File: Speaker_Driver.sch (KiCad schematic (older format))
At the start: 46 parts

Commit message: Annotation has been done
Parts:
- gave numbers to parts that had none: 46

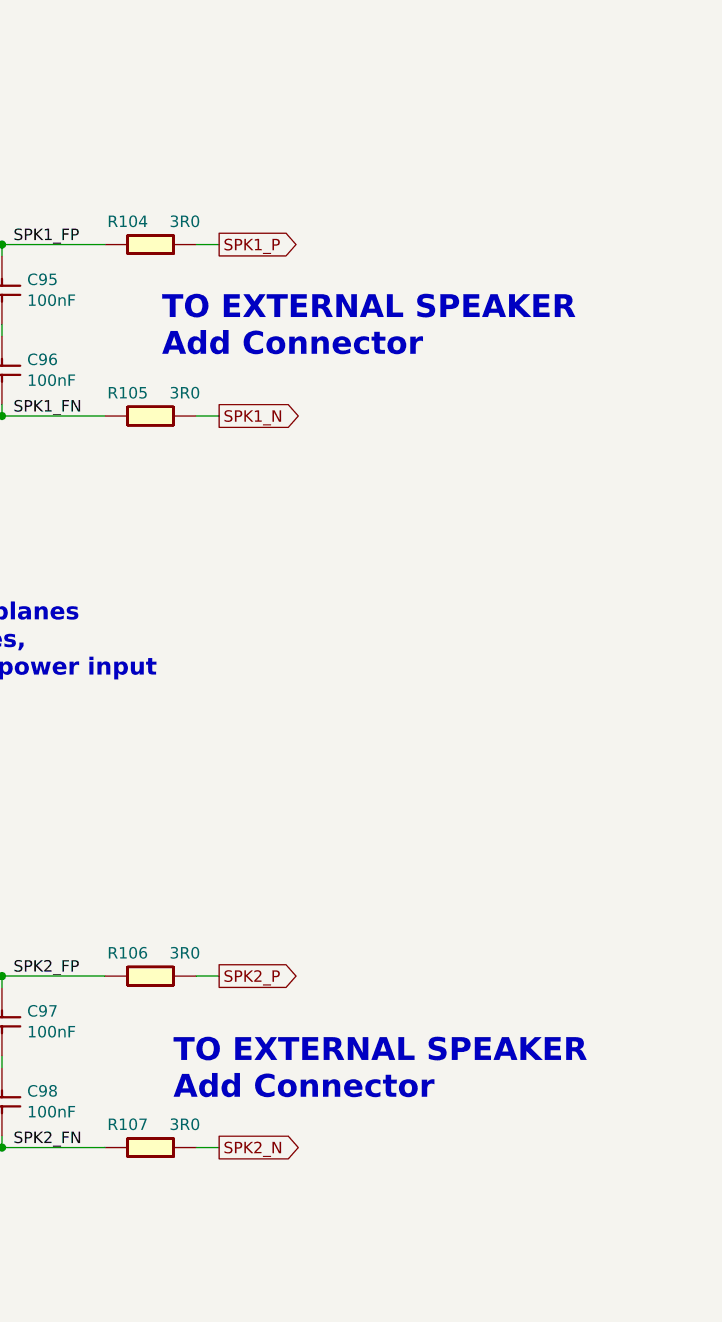
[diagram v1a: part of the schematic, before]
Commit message: added connectors for oxygen sensor and speakers molex 2.54mm pitch vertical
connectors have been added for oxygen sensor and speakers. thery are molex vertical connector 2.54mm pitch vertical. please let me know if any other part is desirable to be used instead.
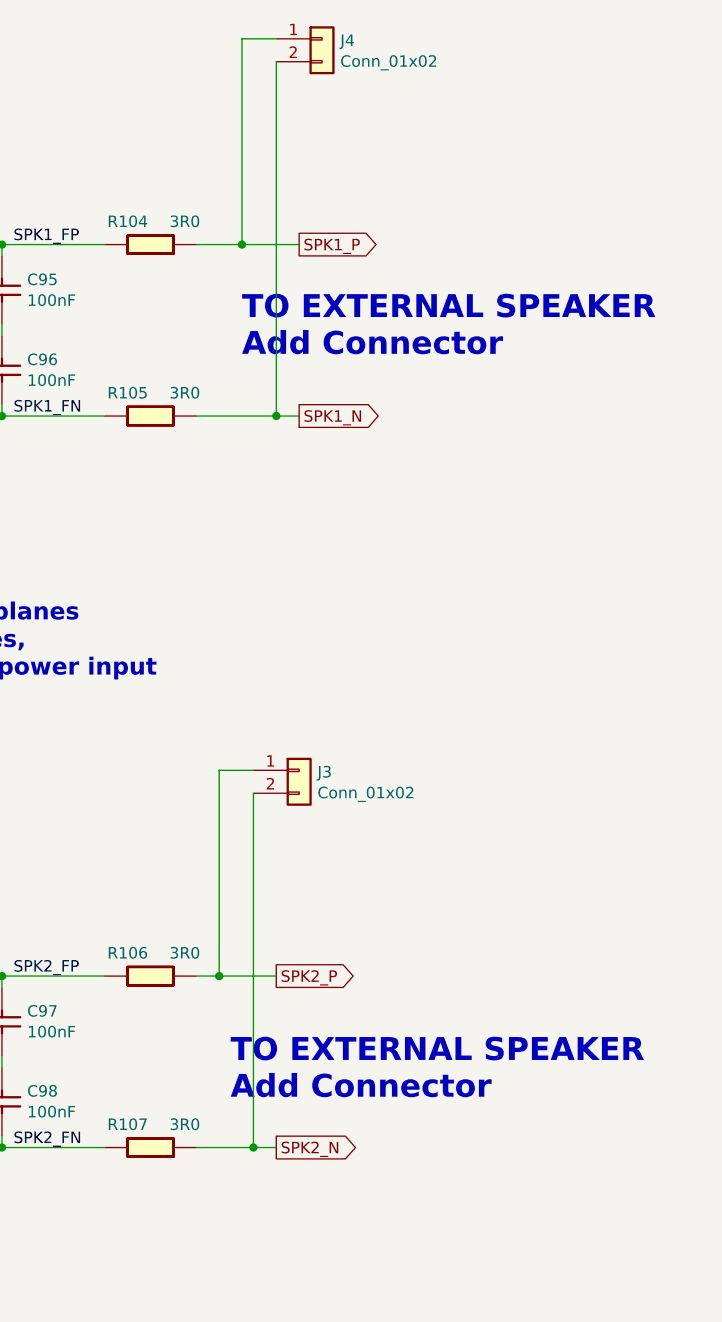
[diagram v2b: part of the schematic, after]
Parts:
- added J3, J4: Conn_01x02, Connector_PinSocket_2.54mm:PinSocket_1x02_P2.54mm_Vertical, symbol Connector_Generic:Conn_01x02
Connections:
- net SPK1_N: now also J4.2 (Pin_2)
- net SPK1_P: now also J4.1 (Pin_1)
- net SPK2_N: now also J3.2 (Pin_2)
- net SPK2_P: now also J3.1 (Pin_1)
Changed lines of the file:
@@
 	1    0    0    -1
 $EndComp
-Text GLabel 9300 1650 2    50   Output ~ 0
+Text GLabel 9650 1650 2    50   Output ~ 0
 SPK1_P
-Text GLabel 9300 2400 2    50   Output ~ 0
+Text GLabel 9650 2400 2    50   Output ~ 0
 SPK1_N
 Wire Wire Line
@@
 Connection ~ 8350 2400
 Wire Wire Line
-	9200 2400 9300 2400
-Wire Wire Line
 	8350 1650 8800 1650
 Connection ~ 8350 1650
-Wire Wire Line
-	9200 1650 9300 1650
 Text Label 8400 1650 0    50   ~ 0
 SPK1_FP
@@
 	1    0    0    -1
 $EndComp
-Text GLabel 9300 4850 2    50   Output ~ 0
+Text GLabel 9550 4850 2    50   Output ~ 0
 SPK2_P
-Text GLabel 9300 5600 2    50   Output ~ 0
+Text GLabel 9550 5600 2    50   Output ~ 0
 SPK2_N
 Wire Wire Line
@@
 Connection ~ 8350 5600
 Wire Wire Line
-	9200 5600 9300 5600
-Wire Wire Line
 	8350 4850 8800 4850
 Connection ~ 8350 4850
-Wire Wire Line
-	9200 4850 9300 4850
 Text Label 8400 4850 0    50   ~ 0
 SPK2_FP
@@
 	1    0    0    -1
 $EndComp
-Text Notes 9050 2150 0    100  ~ 20
+Text Notes 9400 2150 0    100  ~ 20
 TO EXTERNAL SPEAKER\nAdd Connector
 Text Notes 3500 7000 0    50   ~ 0
@@
 	6250 4250 6250 4300
 Connection ~ 6250 4300
-Text Notes 9100 5400 0    100  ~ 20
+Text Notes 9350 5400 0    100  ~ 20
 TO EXTERNAL SPEAKER\nAdd Connector
 Text Notes 600  1650 0    75   ~ 0
@@
 	1    0    0    -1
 $EndComp
+Wire Wire Line
+	9550 750  9400 750
+$Comp
+L Connector_Generic:Conn_01x02 J?
+U 1 1 6093A155
+P 9650 3950
+AR Path="/5F8F3873/6093A155" Ref="J?"  Part="1"
+AR Path="/60D4F569/6093A155" Ref="J3"  Part="1"
+F 0 "J3" H 9730 3942 50  0000 L CNN
+F 1 "Conn_01x02" H 9730 3851 50  0000 L CNN
+F 2 "Connector_PinSocket_2.54mm:PinSocket_1x02_P2.54mm_Vertical" H 9650 3950 50  0001 C CNN
+F 3 "http://www.farnell.com/datasheets/2695416.pdf" H 9650 3950 50  0001 C CNN
+	1    9650 3950
+	1    0    0    -1
+$EndComp
+Wire Wire Line
+	9450 3950 9300 3950
+Wire Wire Line
+	9200 4850 9300 4850
+Wire Wire Line
+	9200 5600 9450 5600
+Wire Wire Line
+	9200 1650 9400 1650
+Wire Wire Line
+	9200 2400 9550 2400
+Wire Wire Line
+	9550 850  9550 2400
+Connection ~ 9550 2400
+Wire Wire Line
+	9550 2400 9650 2400
+Wire Wire Line
+	9400 750  9400 1650
+Connection ~ 9400 1650
+Wire Wire Line
+	9400 1650 9650 1650
+Wire Wire Line
+	9450 4050 9450 5600
+Connection ~ 9450 5600
+Wire Wire Line
+	9450 5600 9550 5600
+Wire Wire Line
+	9300 3950 9300 4850
+Connection ~ 9300 4850
+Wire Wire Line
+	9300 4850 9550 4850
+$Comp
+L Connector_Generic:Conn_01x02 J?
+U 1 1 6099F86B
+P 9750 750
+AR Path="/5F8F3873/6099F86B" Ref="J?"  Part="1"
+AR Path="/60D4F569/6099F86B" Ref="J4"  Part="1"
+F 0 "J4" H 9830 742 50  0000 L CNN
+F 1 "Conn_01x02" H 9830 651 50  0000 L CNN
+F 2 "Connector_PinSocket_2.54mm:PinSocket_1x02_P2.54mm_Vertical" H 9750 750 50  0001 C CNN
+F 3 "http://www.farnell.com/datasheets/2695416.pdf" H 9750 750 50  0001 C CNN
+	1    9750 750
+	1    0    0    -1
+$EndComp

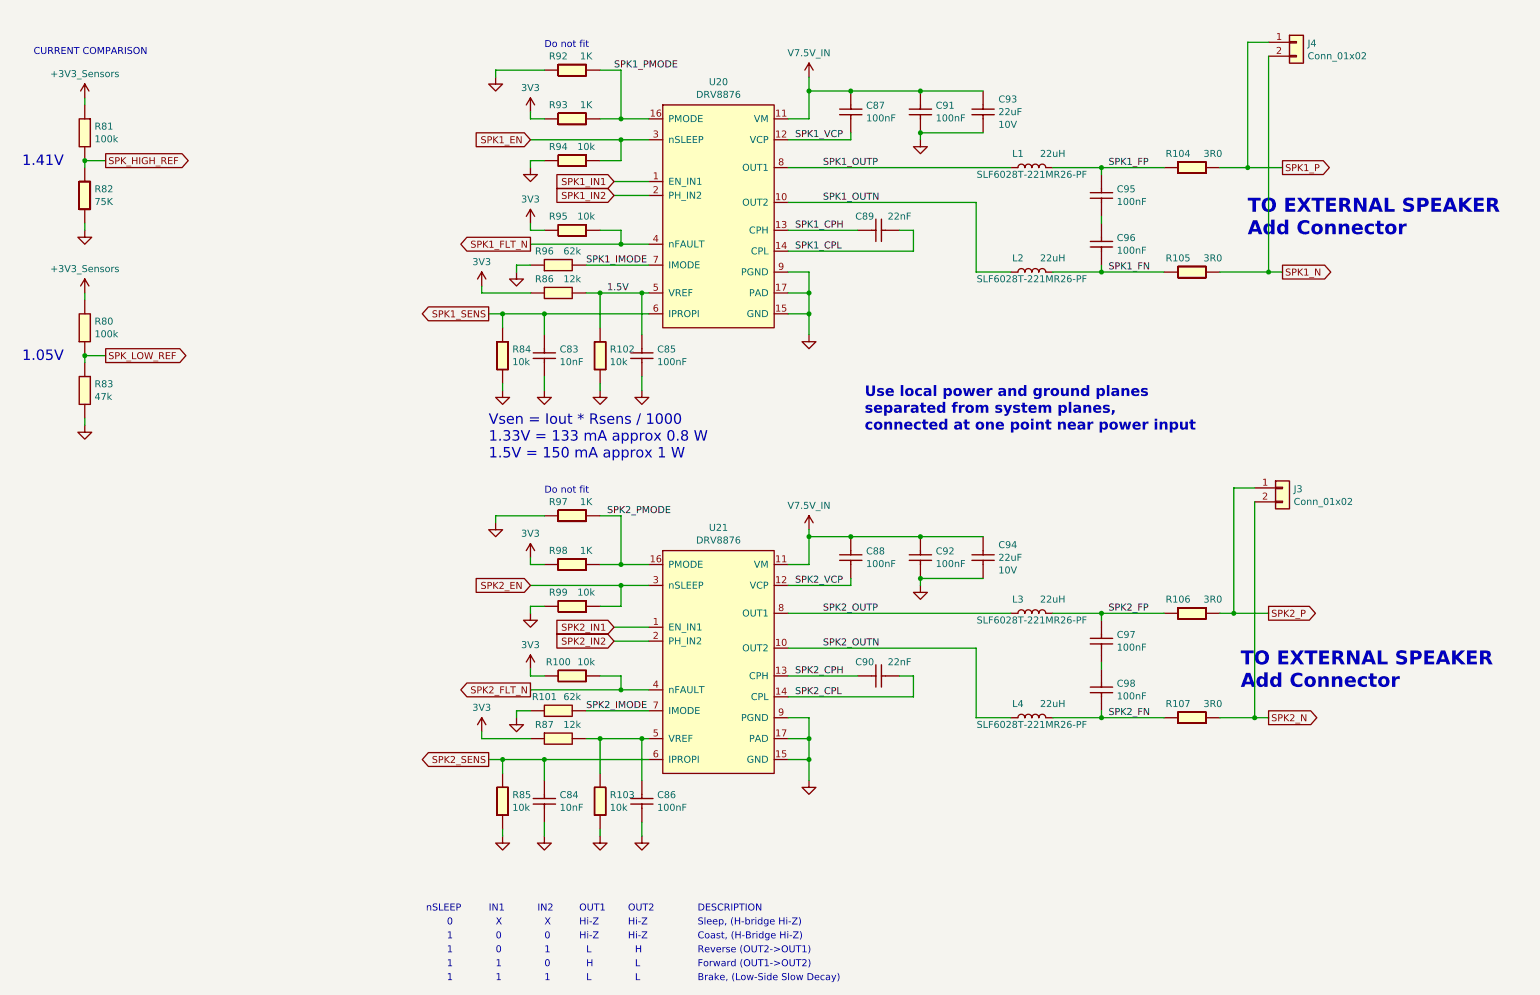
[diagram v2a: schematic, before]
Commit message: Task OEF-413 added zero ohm jumpers for 5V and 7.5V power supply to speaker driver circuits
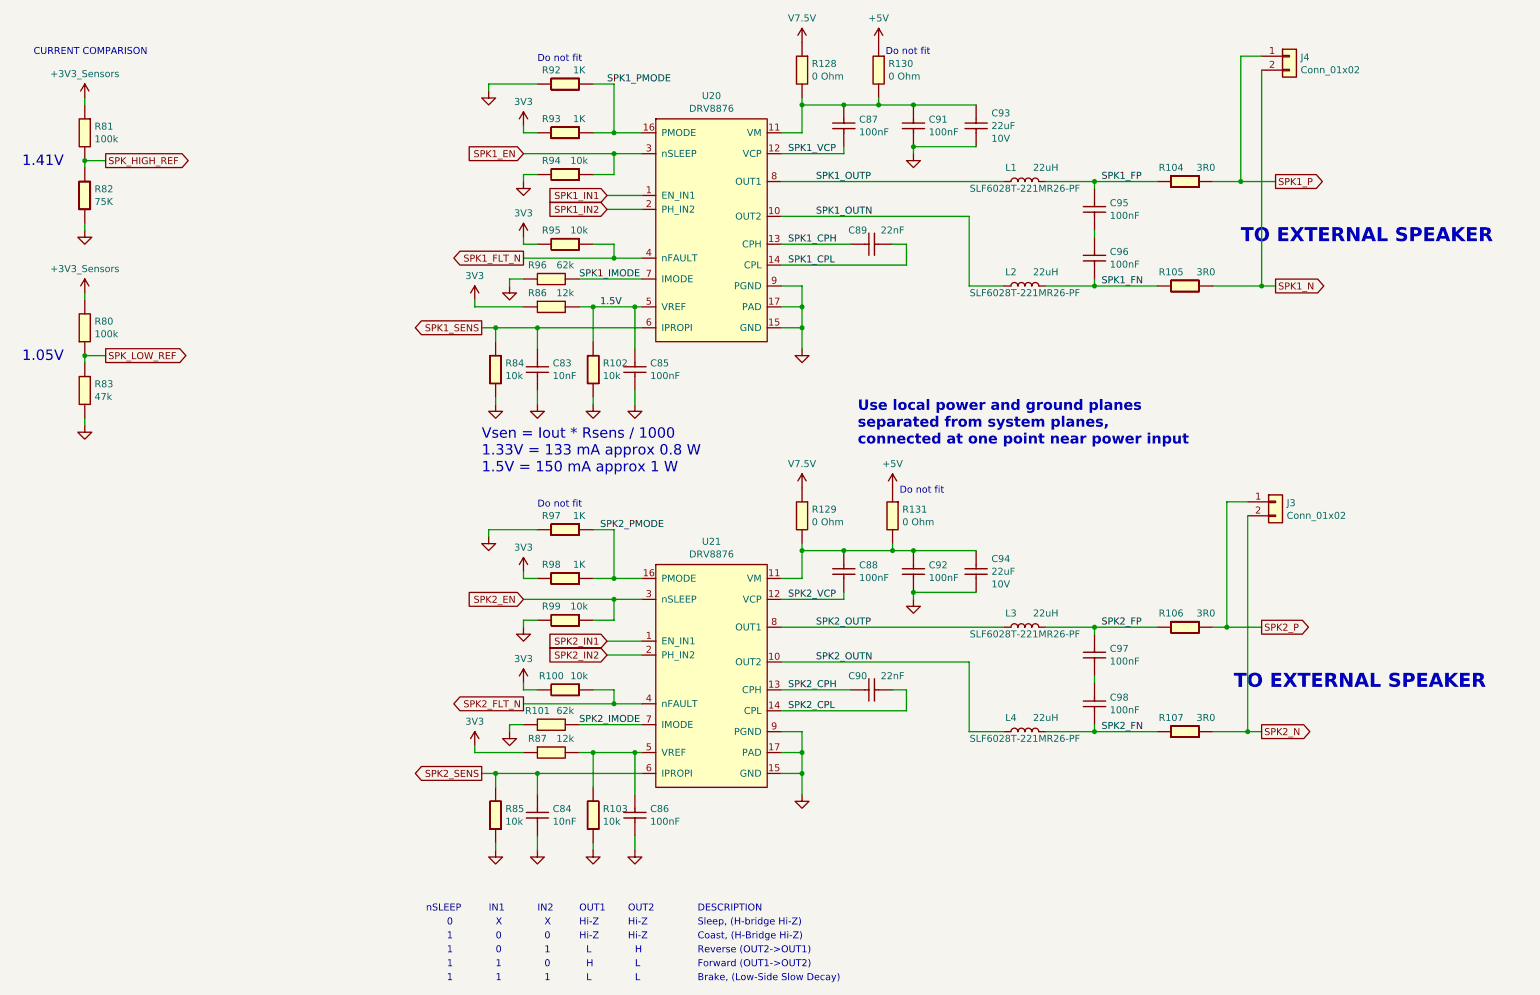
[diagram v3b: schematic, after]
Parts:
- added R128, R129, R130, R131: 0R0_0603_Chip_Resistor,_1%,_0.1W, symbol OpenVent:0R0_0603_Chip_Resistor,_1%,_0.1W
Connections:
- net +5V: now also R128.1, R129.1, R130.1, R131.1; no longer C87.1, C88.1, C91.1, C92.1, C93.1, C94.1, U20.11 (VM), U21.11 (VM)
- new net: C87.1, C91.1, C93.1, R128.2, R130.2, U20.11 (VM)
- new net: C88.1, C92.1, C94.1, R129.2, R131.2, U21.11 (VM)
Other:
- note added: "TO EXTERNAL SPEAKER"
- note removed: "TO EXTERNAL SPEAKER\nAdd Connector"
- moved on the sheet: C83, C84, C85, C86, C87, C88, C89, C90, C91, C92, C93, C94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

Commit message: footprint added to 99%
99% of parts have footprint now.
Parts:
- L3, L4: footprint (none) -> OpenVent_Footprint_Test:SLF6028T-221MR26-PF
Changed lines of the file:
@@
 F 0 "L3" H 7700 5050 50  0000 C CNN
 F 1 "SLF6028T-221MR26-PF" H 7800 4900 50  0000 C CNN
-F 2 "" V 7800 4950 50  0001 C CNN
+F 2 "OpenVent_Footprint_Test:SLF6028T-221MR26-PF" V 7800 4950 50  0001 C CNN
 F 3 "https://drive.google.com/drive/u/1/folders/1bT0MezjjDfDXdTdQktjf6O5y5oTJs8ND" V 7800 4950 50  0001 C CNN
 F 4 "TDK" H 7700 4800 50  0001 C CNN "Mfr"
@@
 F 0 "L4" H 7700 5800 50  0000 C CNN
 F 1 "SLF6028T-221MR26-PF" H 7800 5650 50  0000 C CNN
-F 2 "" V 7800 5700 50  0001 C CNN
+F 2 "OpenVent_Footprint_Test:SLF6028T-221MR26-PF" V 7800 5700 50  0001 C CNN
 F 3 "https://drive.google.com/drive/u/1/folders/1bT0MezjjDfDXdTdQktjf6O5y5oTJs8ND" V 7800 5700 50  0001 C CNN
 F 4 "TDK" H 7700 5550 50  0001 C CNN "Mfr"

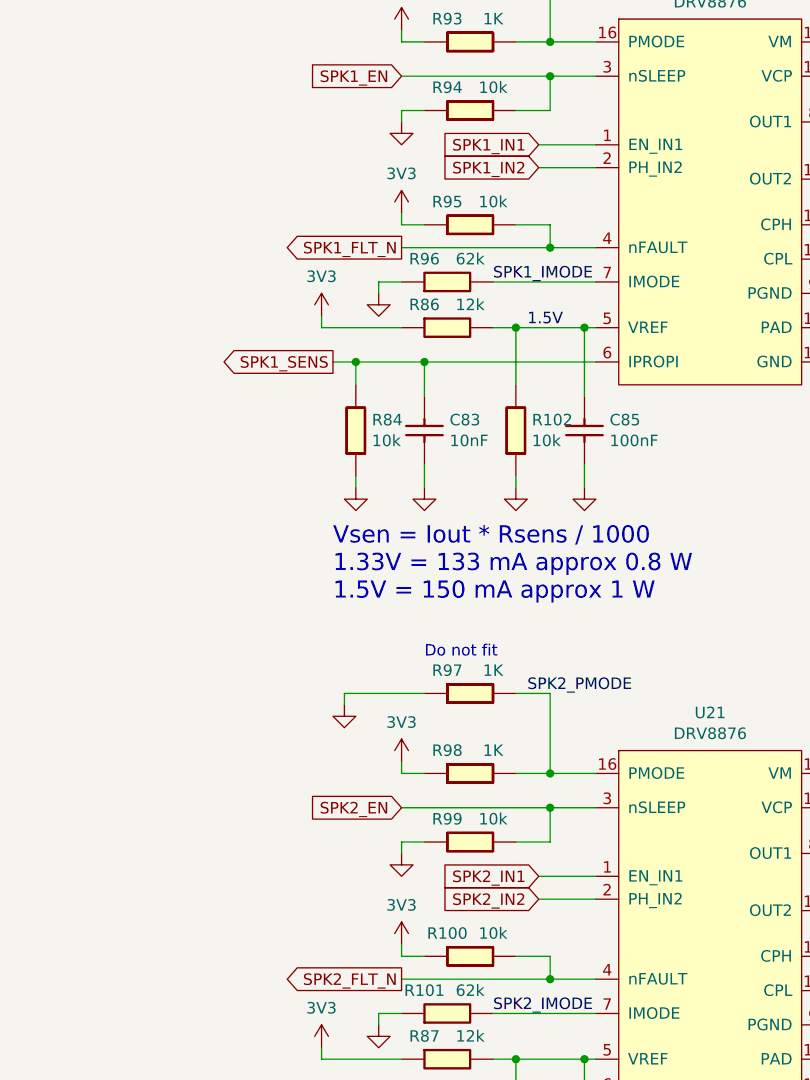
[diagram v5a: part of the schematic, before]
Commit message: Finalised most of the schematic. I think there are a few more things to do in the Speaker
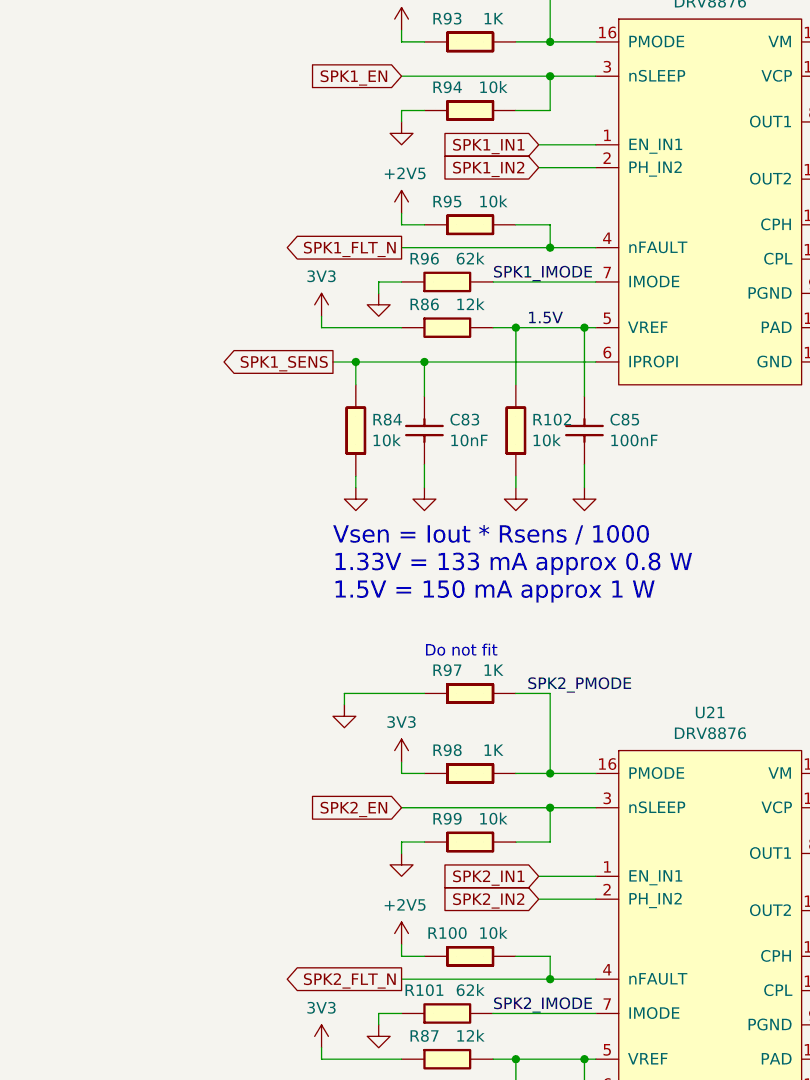
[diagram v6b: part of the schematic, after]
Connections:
- net +3V3: no longer R100.1, R95.1
- new net +2V5: R100.1, R95.1
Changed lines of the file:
@@
 EESchema Schematic File Version 4
-LIBS:OpenVent-cache
-EELAYER 26 0
+EELAYER 30 0
 EELAYER END
 $Descr A4 11693 8268
 encoding utf-8
-Sheet 7 9
+Sheet 6 9
 Title ""
 Date ""
@@
 	4850 1550 4200 1550
 Connection ~ 4850 1550
-$Comp
-L OpenVent:3V3 #PWR0142
-U 1 1 6072AB3F
-P 4200 2150
-F 0 "#PWR0142" H 4200 2000 50  0001 C CNN
-F 1 "3V3" H 4200 2323 50  0000 C CNN
-F 2 "" H 4200 2150 50  0001 C CNN
-F 3 "" H 4200 2150 50  0001 C CNN
-	1    4200 2150
-	1    0    0    -1
-$EndComp
 Wire Wire Line
 	4300 1400 4200 1400
@@
 	4850 4750 4200 4750
 Connection ~ 4850 4750
-$Comp
-L OpenVent:3V3 #PWR0145
-U 1 1 607E3370
-P 4200 5350
-F 0 "#PWR0145" H 4200 5200 50  0001 C CNN
-F 1 "3V3" H 4200 5523 50  0000 C CNN
-F 2 "" H 4200 5350 50  0001 C CNN
-F 3 "" H 4200 5350 50  0001 C CNN
-	1    4200 5350
-	1    0    0    -1
-$EndComp
 Wire Wire Line
 	4300 4600 4200 4600
@@
 Text Notes 6900 4000 0    50   ~ 0
 Do not fit
+$Comp
+L power:+2V5 #PWR?
+U 1 1 625BD691
+P 4200 2150
+AR Path="/5F99D63D/625BD691" Ref="#PWR?"  Part="1"
+AR Path="/5FCA4074/625BD691" Ref="#PWR?"  Part="1"
+AR Path="/60D4F569/625BD691" Ref="#PWR?"  Part="1"
+F 0 "#PWR?" H 4200 2000 50  0001 C CNN
+F 1 "+2V5" H 4215 2323 50  0000 C CNN
+F 2 "" H 4200 2150 50  0001 C CNN
+F 3 "" H 4200 2150 50  0001 C CNN
+	1    4200 2150
+	1    0    0    -1
+$EndComp
+$Comp
+L power:+2V5 #PWR?
+U 1 1 625C511B
+P 4200 5350
+AR Path="/5F99D63D/625C511B" Ref="#PWR?"  Part="1"
+AR Path="/5FCA4074/625C511B" Ref="#PWR?"  Part="1"
+AR Path="/60D4F569/625C511B" Ref="#PWR?"  Part="1"
+F 0 "#PWR?" H 4200 5200 50  0001 C CNN
+F 1 "+2V5" H 4215 5523 50  0000 C CNN
+F 2 "" H 4200 5350 50  0001 C CNN
+F 3 "" H 4200 5350 50  0001 C CNN
+	1    4200 5350
+	1    0    0    -1
+$EndComp
 $EndSCHEMATC
